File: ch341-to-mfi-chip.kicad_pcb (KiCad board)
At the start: 2 copper layers, 23.5 x 18.4 mm, 14 parts, among them J1 USB-212-BCW, U1 CH341F, U2 HR1117V-3.3, U3 MFI337S3959

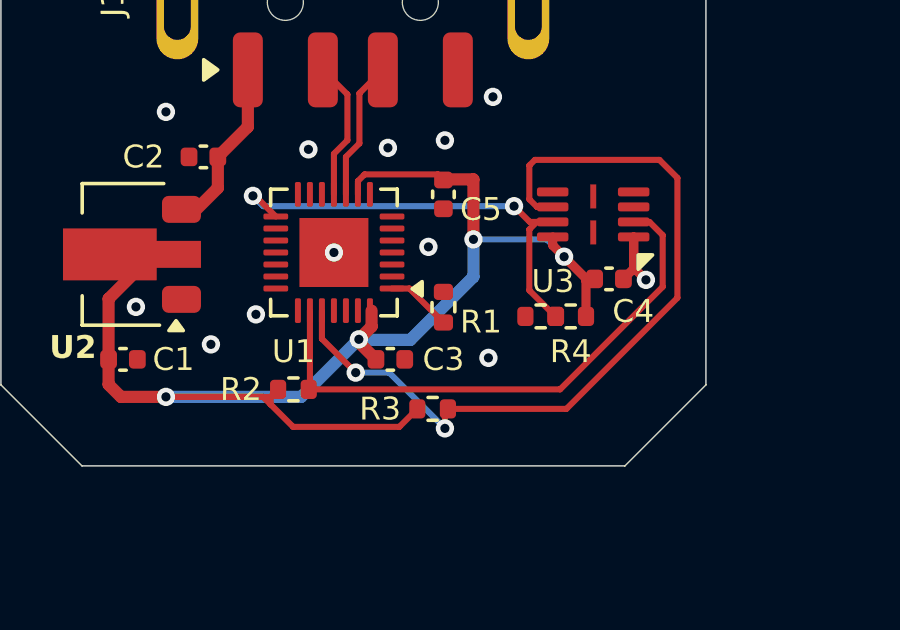
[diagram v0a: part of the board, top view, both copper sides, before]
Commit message: change position of R1
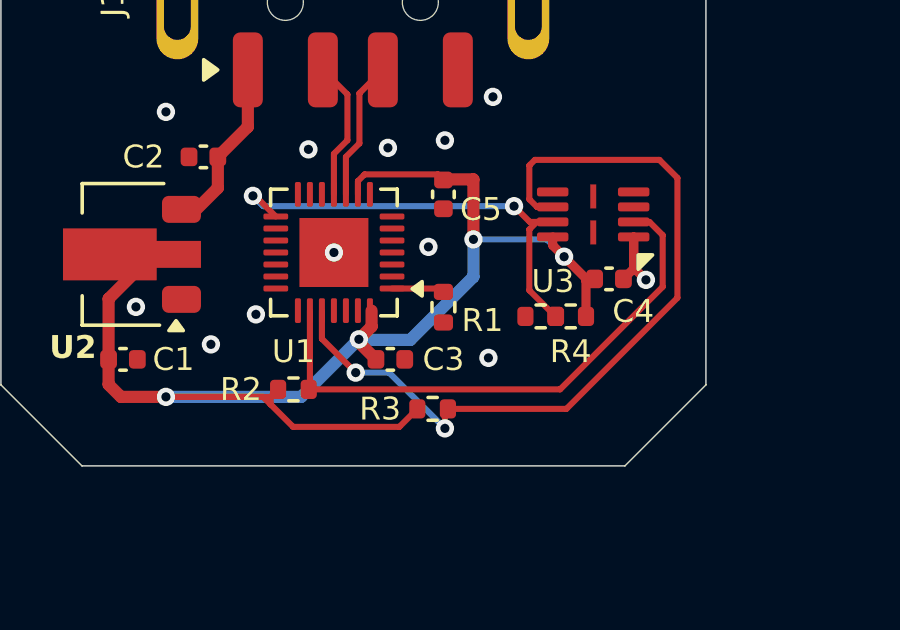
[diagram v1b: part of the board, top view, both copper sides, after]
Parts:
- turned R1 to -90 degrees
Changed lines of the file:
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@@
 	(footprint "Resistor_SMD:R_0402_1005Metric"
 		(layer "F.Cu")
-		(at 78 51.26 90)
+		(at 78 51.26 -90)
 		(descr "Resistor SMD 0402 (1005 Metric), square (rectangular) end terminal, IPC-7351 nominal, (Body size source: IPC-SM-782 page 72, https://www.pcb-3d.com/wordpress/wp-content/uploads/ipc-sm-782a_amendment_1_and_2.pdf)")
 		(tags "resistor")
 		(property "Reference" "R1"
-			(at -0.49 1.25 180)
+			(at 0.44 -1.3 0)
 			(layer "F.SilkS")
 			(effects
@@
 		(duplicate_pad_numbers_are_jumpers no)
 		(fp_line
+			(start -0.153641 0.38)
+			(end 0.153641 0.38)
+			(stroke
+				(width 0.12)
+				(type solid)
+			)
+			(layer "F.SilkS")
+		)
+		(fp_line
 			(start -0.153641 -0.38)
 			(end 0.153641 -0.38)
-			(stroke
-				(width 0.12)
-				(type solid)
-			)
-			(layer "F.SilkS")
-		)
-		(fp_line
-			(start -0.153641 0.38)
-			(end 0.153641 0.38)
 			(stroke
 				(width 0.12)
@@
 		)
 		(pad "1" smd roundrect
-			(at -0.51 0 90)
+			(at -0.51 0 270)
 			(size 0.54 0.64)
 			(layers "F.Cu" "F.Mask" "F.Paste")
@@
 		)
 		(pad "2" smd roundrect
-			(at 0.51 0 90)
+			(at 0.51 0 270)
 			(size 0.54 0.64)
 			(layers "F.Cu" "F.Mask" "F.Paste")
@@
 	)
 	(segment
+		(start 77.8875 50.6375)
+		(end 78 50.75)
+		(width 0.2032)
+		(layer "F.Cu")
+		(net "Net-(U1-ACT#)")
+	)
+	(segment
 		(start 76.2875 50.6375)
-		(end 76.8675 50.6375)
-		(width 0.2032)
-		(layer "F.Cu")
-		(net "Net-(U1-ACT#)")
-	)
-	(segment
-		(start 76.8675 50.6375)
-		(end 78 51.77)
-		(width 0.2032)
-		(layer "F.Cu")
+		(end 77.8875 50.6375)
+		(width 0.2032)
+		(layer "F.Cu")

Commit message: now better
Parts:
- added G***: LOGO, KicadLibrary:GITHUB LOGO, F.Cu at (67.1, 54.4)
- moved C2 3.84 mm to (66.5, 44.8)
- moved R3 2.11 mm to (76.2, 53.1), turned to 180 degrees
- moved R2 1.94 mm to (73.3, 52.1)
- moved R5 1.80 mm to (83.0, 51.9), turned to 0 degrees
- moved C4 1.57 mm to (82.0, 50.9)
- moved R1 1.55 mm to (78.5, 49.8)
- moved U2 1.24 mm to (68.4, 48.9), turned to -90 degrees
- moved U1 1.13 mm to (74.8, 48.4)
- moved C3 0.93 mm to (76.2, 52.1)
- moved C1 0.91 mm to (66.8, 52.2), turned to 180 degrees
- moved C5 0.64 mm to (78.5, 47.9)
- moved U3 0.62 mm to (82.5, 48.6)
- moved R4 0.36 mm to (82.0, 51.9), turned to 0 degrees
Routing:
- net Net-(U1-SCL): track 27.4 -> 13.1 mm, vias 2 -> 0
- net Net-(U1-CS0): track 15.5 -> 26.8 mm
- net GND: track 3.14 -> 0.00 mm, vias 12 -> 13
- net Net-(J1-VBUS): track 5.36 -> 7.39 mm
- net +3V3: track 49.9 -> 48.2 mm, vias 4 -> 5
- net /USB_D-: track 4.68 -> 3.46 mm
- net /USB_D+: track 4.66 -> 3.46 mm
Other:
- board text added: "RST"
- board text added: "Shilapi"
